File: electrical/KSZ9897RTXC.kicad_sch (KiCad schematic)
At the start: 2 parts, among them U1 KSZ9897RTXC

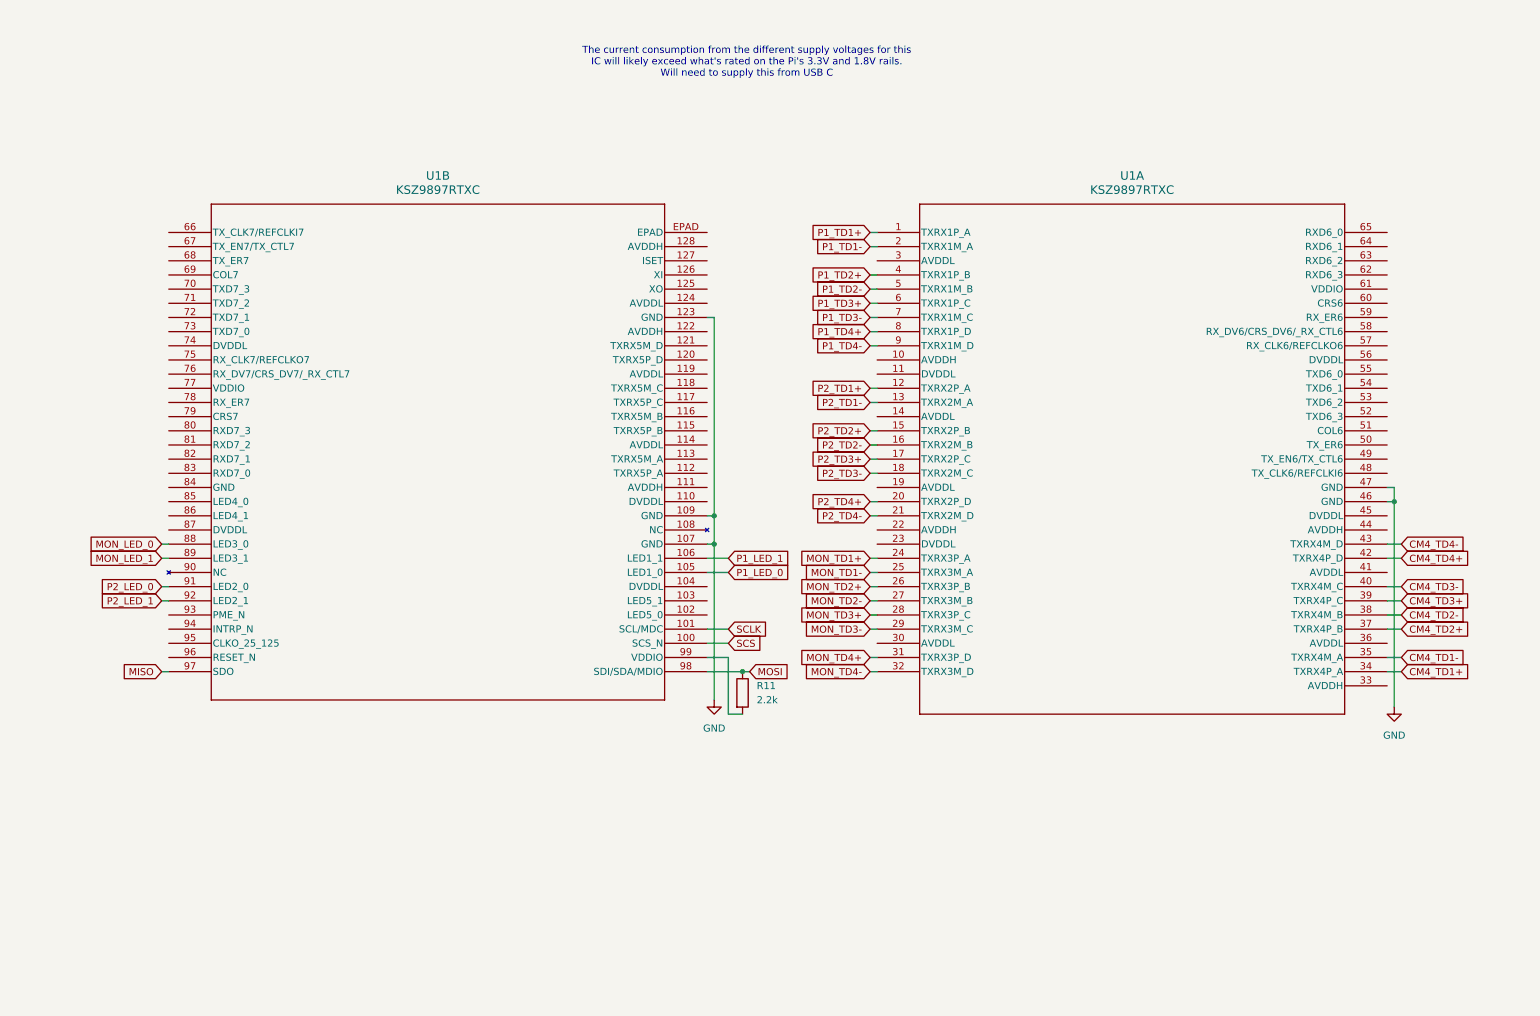
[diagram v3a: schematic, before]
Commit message: KSZ9897 Power
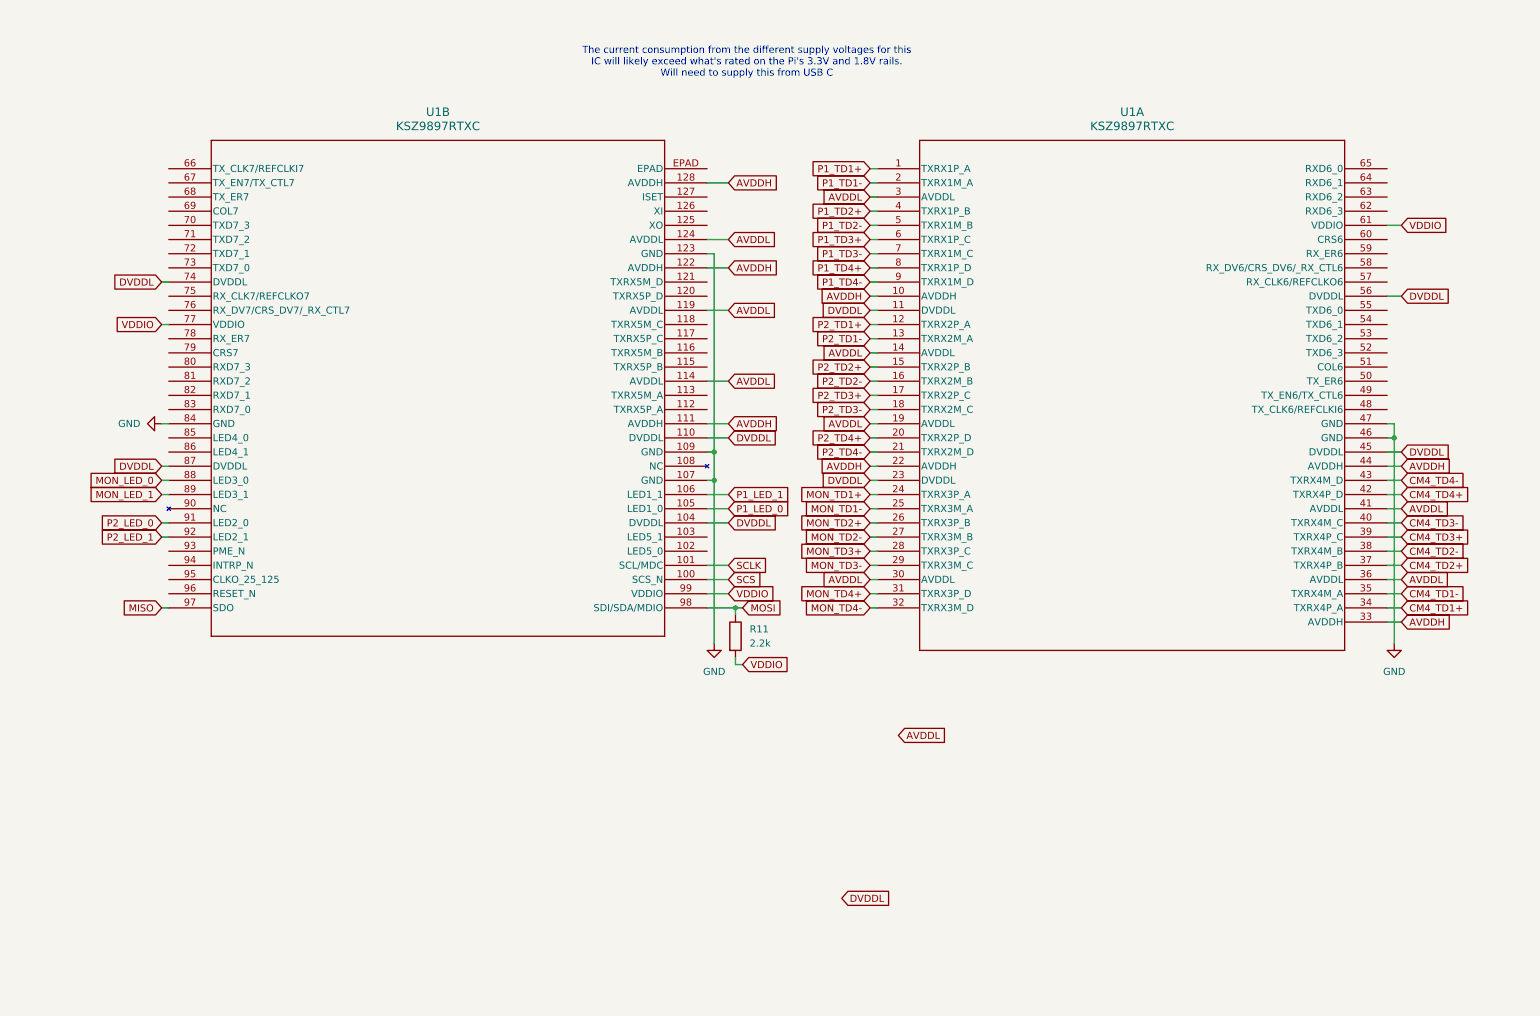
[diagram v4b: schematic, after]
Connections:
- net GND: now also U1.84 (GND)
- net VDDIO: now reaches R11.2, U1.99 (VDDIO)
- net VDDIO: now also U1.61 (VDDIO), U1.77 (VDDIO)
- net AVDDH: now reaches U1.10 (AVDDH)
- net AVDDH: now also U1.111 (AVDDH), U1.122 (AVDDH), U1.128 (AVDDH), U1.22 (AVDDH), U1.33 (AVDDH), U1.44 (AVDDH)
- net DVDDL: now reaches U1.11 (DVDDL)
- net DVDDL: now also U1.104 (DVDDL), U1.110 (DVDDL), U1.23 (DVDDL), U1.45 (DVDDL), U1.56 (DVDDL), U1.74 (DVDDL), U1.87 (DVDDL)
- net AVDDL: now reaches U1.14 (AVDDL)
- net AVDDL: now also U1.114 (AVDDL), U1.119 (AVDDL), U1.124 (AVDDL), U1.19 (AVDDL), U1.3 (AVDDL), U1.30 (AVDDL), U1.36 (AVDDL), U1.41 (AVDDL)
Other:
- moved on the sheet: R11, U1A, U1B

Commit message: 25MHz crystal for KSZ9897
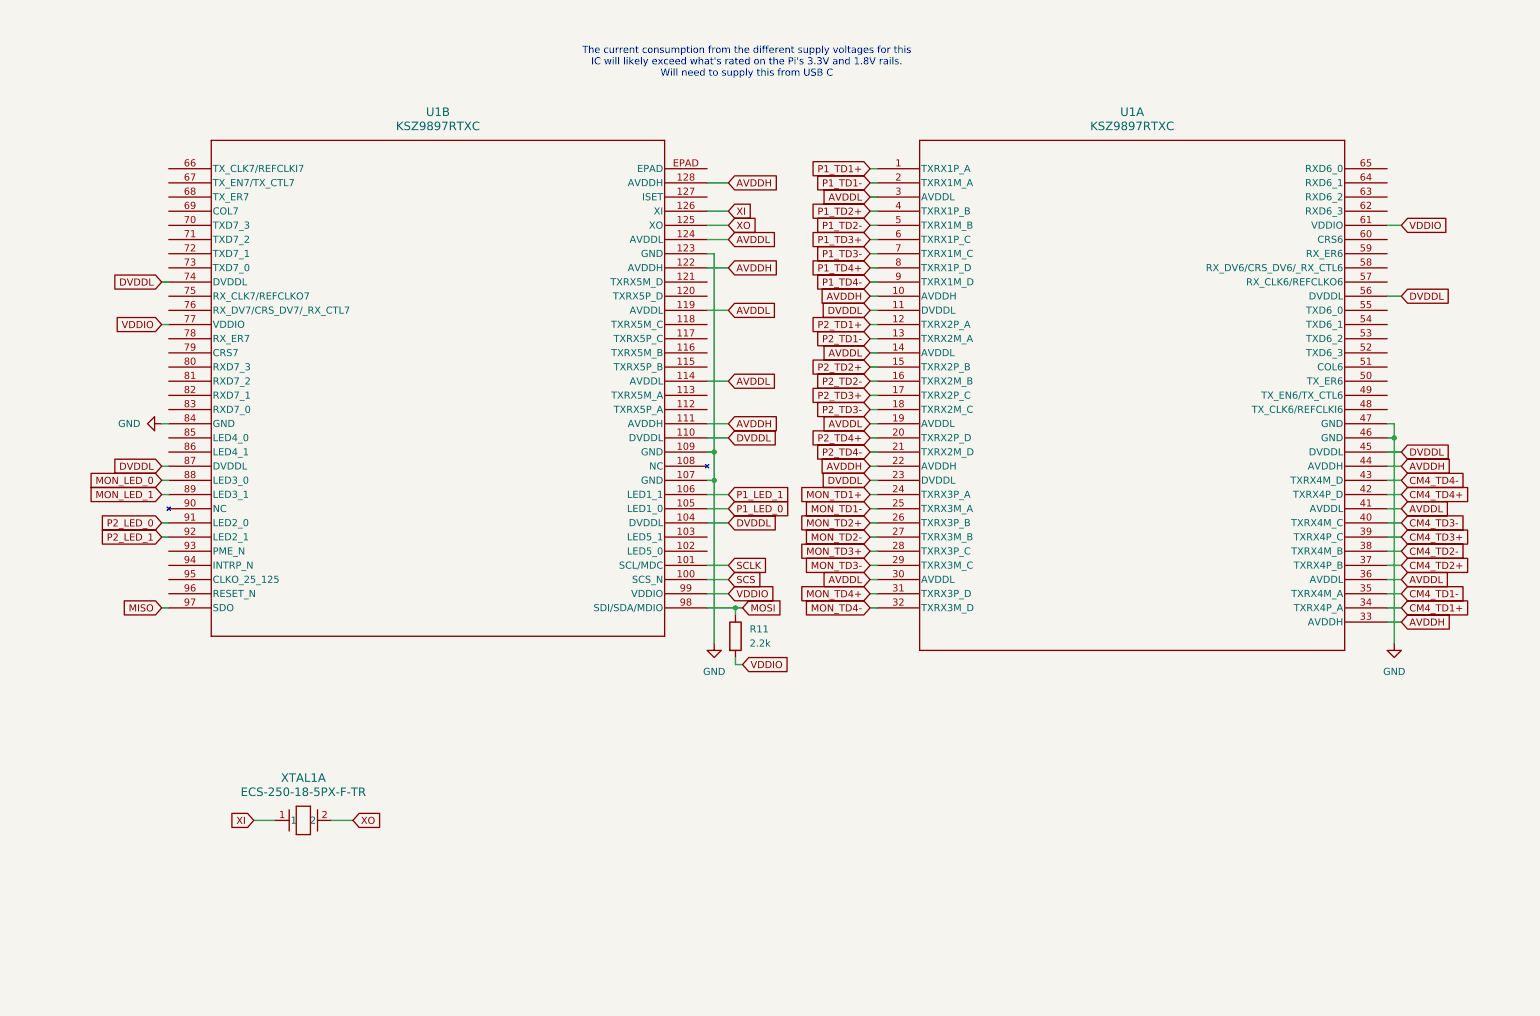
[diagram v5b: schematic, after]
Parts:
- added XTAL1: ECS-250-18-5PX-F-TR, CRYSTAL_ECS-250-18-5PX-F-TR_ECS, symbol ECS-250-18-5PX-F-TR:ECS-250-18-5PX-F-TR
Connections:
- net XO: now reaches U1.125 (XO)
- net XO: now also XTAL1.2
- net XI: now reaches U1.126 (XI)
- net XI: now also XTAL1.1

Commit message: 2V5, 1V2 Buck converters
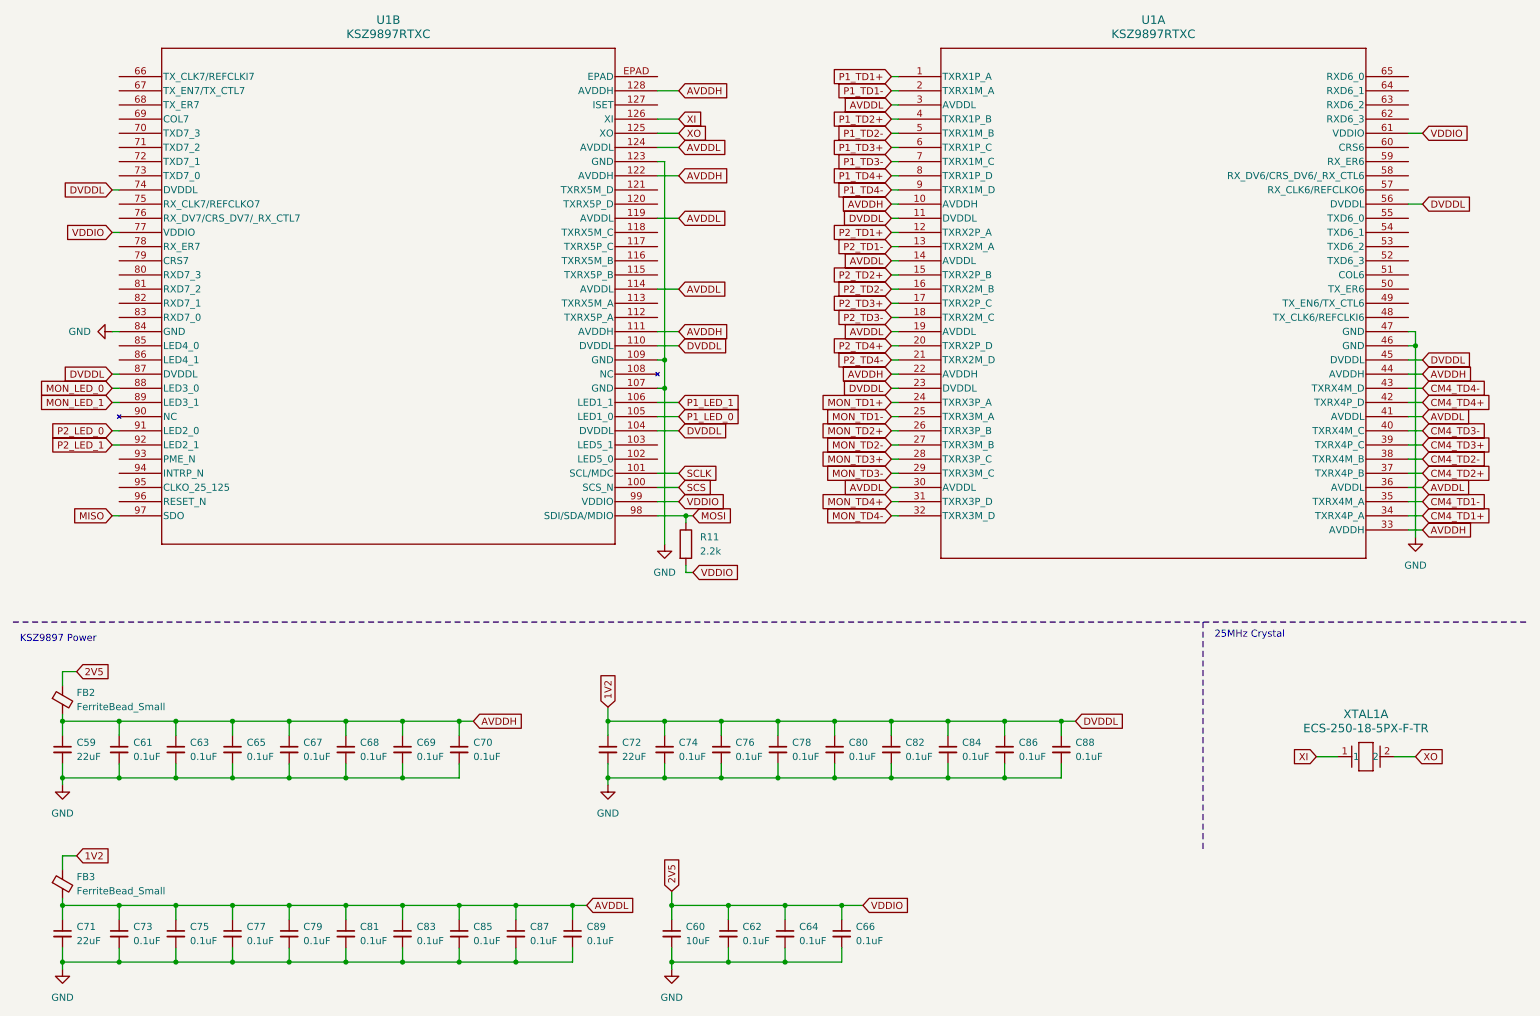
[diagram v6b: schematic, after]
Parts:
- added C59, C71, C72: 22uF, symbol Device:C_Small
- added C60: 10uF, symbol Device:C_Small
- added C61, C62, C63, C64, C65, C66, C67, C68, C69, C70, C73, C74, C75, C76, C77, C78, C79, C80, C81, C82, C83, C84, C85, C86, C87, C88, C89: 0.1uF, symbol Device:C_Small
- added FB2, FB3: FerriteBead_Small, symbol Device:FerriteBead_Small
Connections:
- net AVDDH: now also C59.1, C61.1, C63.1, C65.1, C67.1, C68.1, C69.1, C70.1, FB2.2
- net AVDDL: now also C71.1, C73.1, C75.1, C77.1, C79.1, C81.1, C83.1, C85.1, C87.1, C89.1, FB3.2
- net GND: now also C59.2, C60.2, C61.2, C62.2, C63.2, C64.2, C65.2, C66.2, C67.2, C68.2, C69.2, C70.2, C71.2, C72.2, C73.2, C74.2, C75.2, C76.2, C77.2, C78.2, C79.2, C80.2, C81.2, C82.2, C83.2, C84.2, C85.2, C86.2, C87.2, C88.2, C89.2
- net DVDDL renamed 1V2
- net 1V2: now also C72.1, C74.1, C76.1, C78.1, C80.1, C82.1, C84.1, C86.1, C88.1, FB3.1
- net VDDIO renamed 2V5
- net 2V5: now also C60.1, C62.1, C64.1, C66.1, FB2.1
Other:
- note added: "25MHz Crystal"
- note added: "KSZ9897 Power"
- note removed: "The current consumption from the different supply voltages for this IC will likely exceed what's rated on the Pi's 3.3V and 1.8V rails. Will need to supply this from USB C"
- moved on the sheet: R11, U1A, U1B, XTAL1A

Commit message: Micro B + Header for eMMC flash
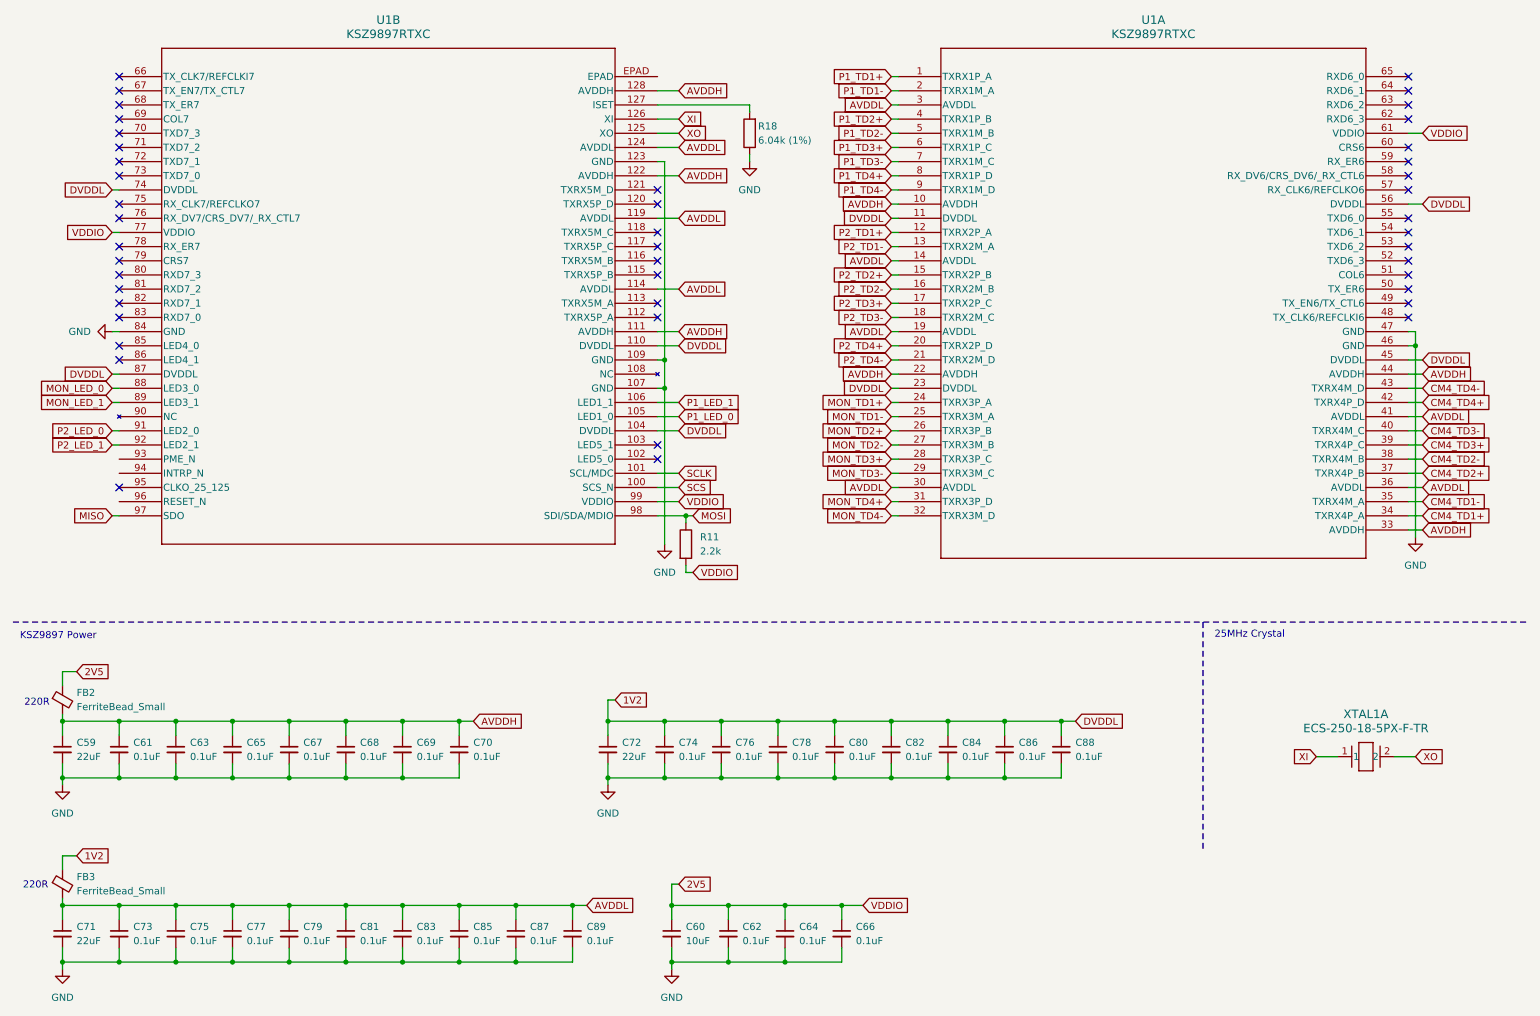
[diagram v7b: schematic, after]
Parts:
- added R18: 6.04k (1%), symbol Device:R
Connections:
- net GND: now also R18.1
- net at U1.127 (ISET): now also R18.2
- no-connect marks 0 -> 45
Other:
- note added: "220R"
- title: (none) -> Network Tap
